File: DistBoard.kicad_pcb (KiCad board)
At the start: 2 copper layers, 63.6 x 50.8 mm, 21 parts, among them J1 22-27-2021, J2 Conn_01x03, J3 Conn_01x03, J4 Conn_01x03, J5 Conn_01x03, U1 TLE2426CDR

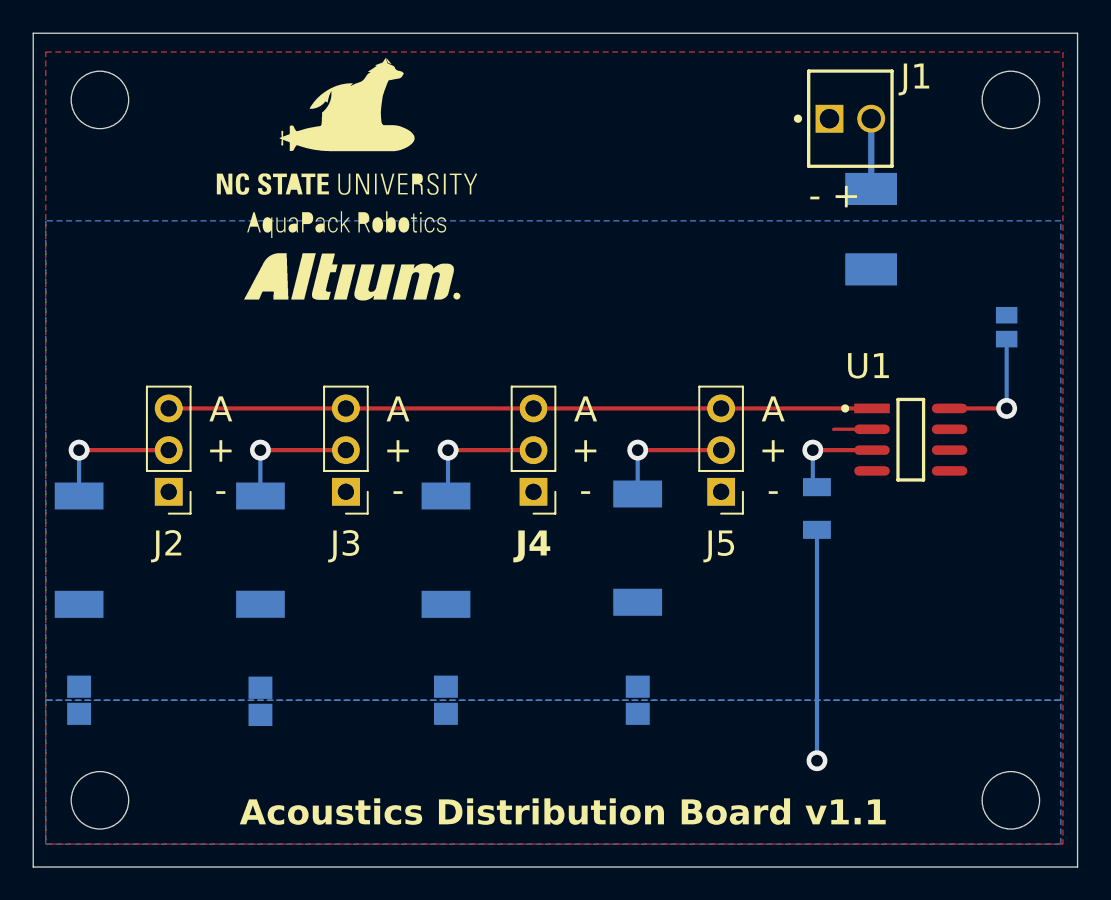
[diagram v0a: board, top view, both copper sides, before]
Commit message: Swap to socket headers and fix drc violations
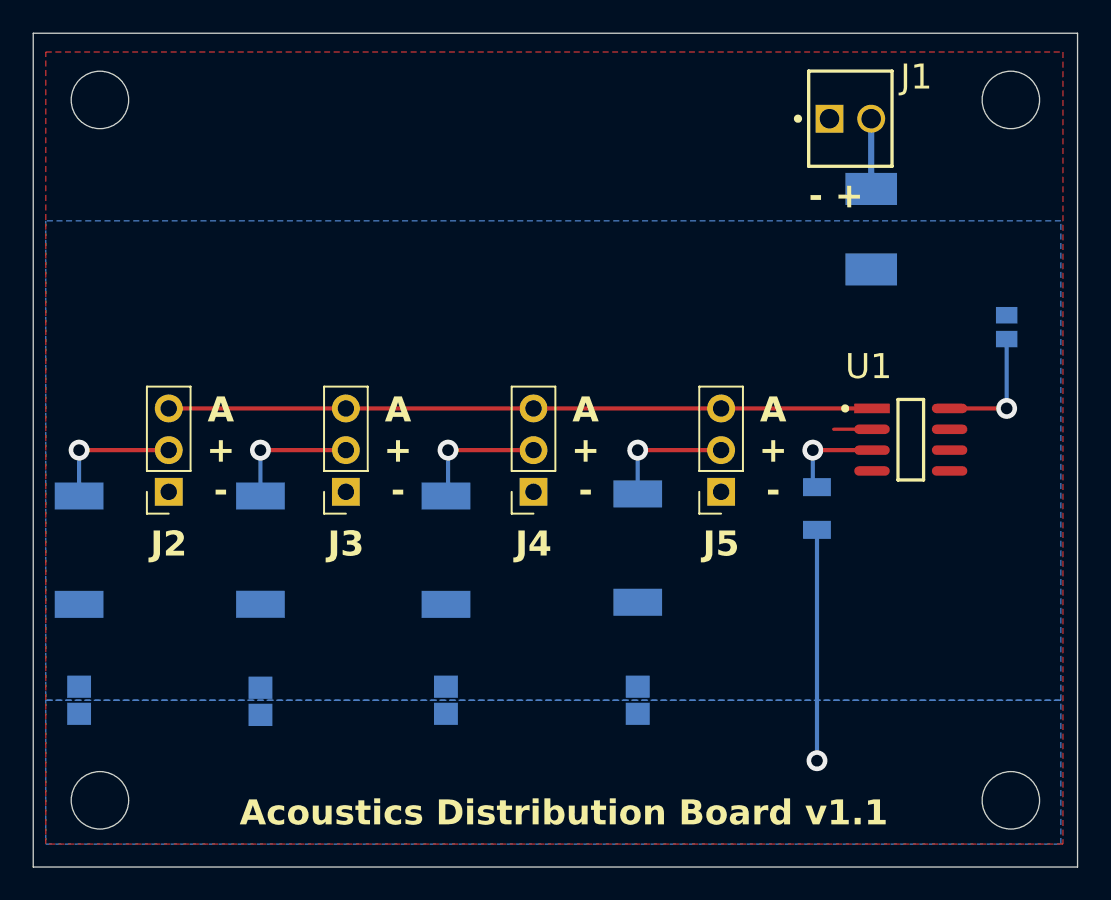
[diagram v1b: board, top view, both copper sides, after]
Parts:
- J2, J3, J4, J5: footprint Connector_PinHeader_2.54mm:PinHeader_1x03_P2.54mm_Vertical -> Connector_PinSocket_2.54mm:PinSocket_1x03_P2.54mm_Vertical

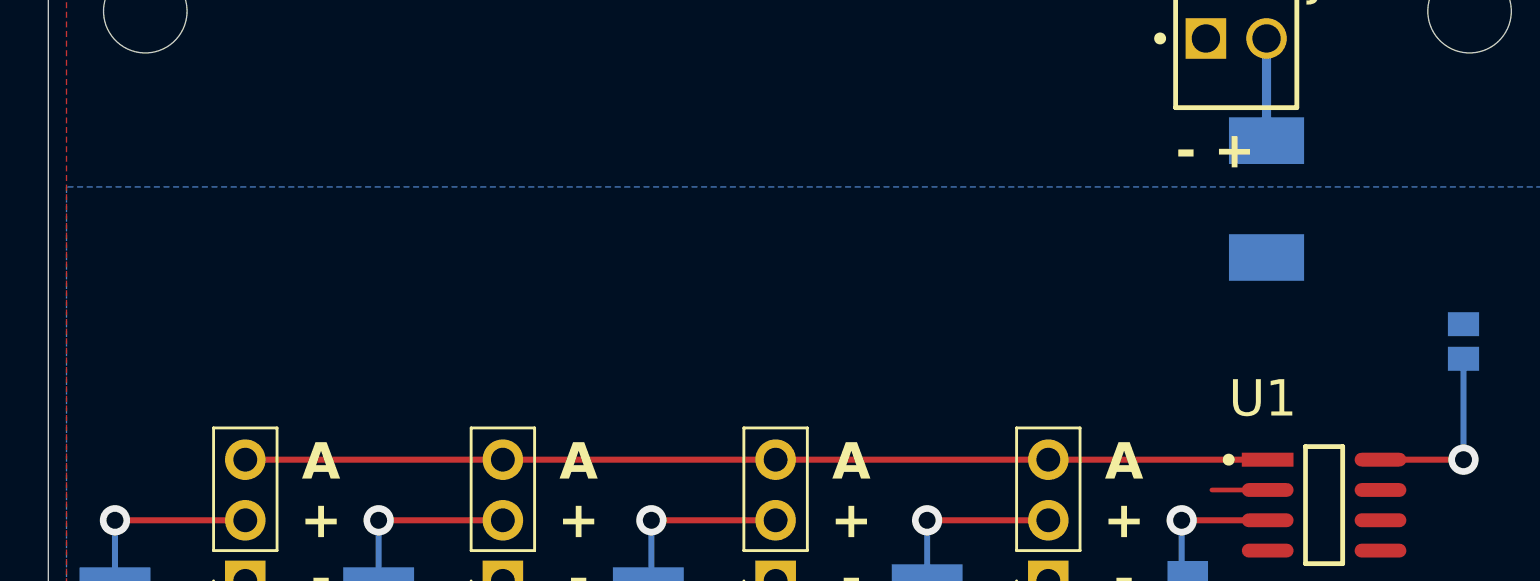
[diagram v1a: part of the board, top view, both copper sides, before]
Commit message: Add logos
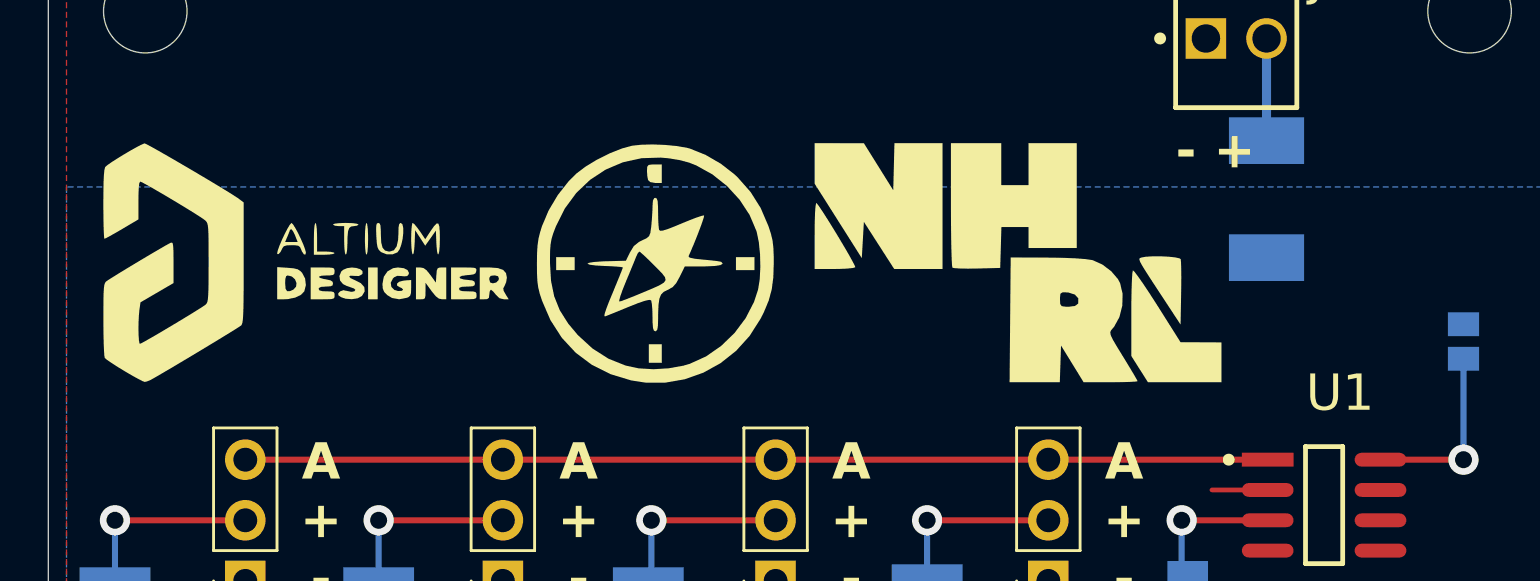
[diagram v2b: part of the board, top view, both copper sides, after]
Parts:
- added G***: LOGO, LOGO, F.Cu at (142.1, 94.2)
- added G***: LOGO, LOGO, F.Cu at (127.5, 94.2)
- added G***: LOGO, LOGO, F.Cu at (157.3, 94.2)
- added G***: LOGO, LOGO, B.Cu at (142.1, 89.1)

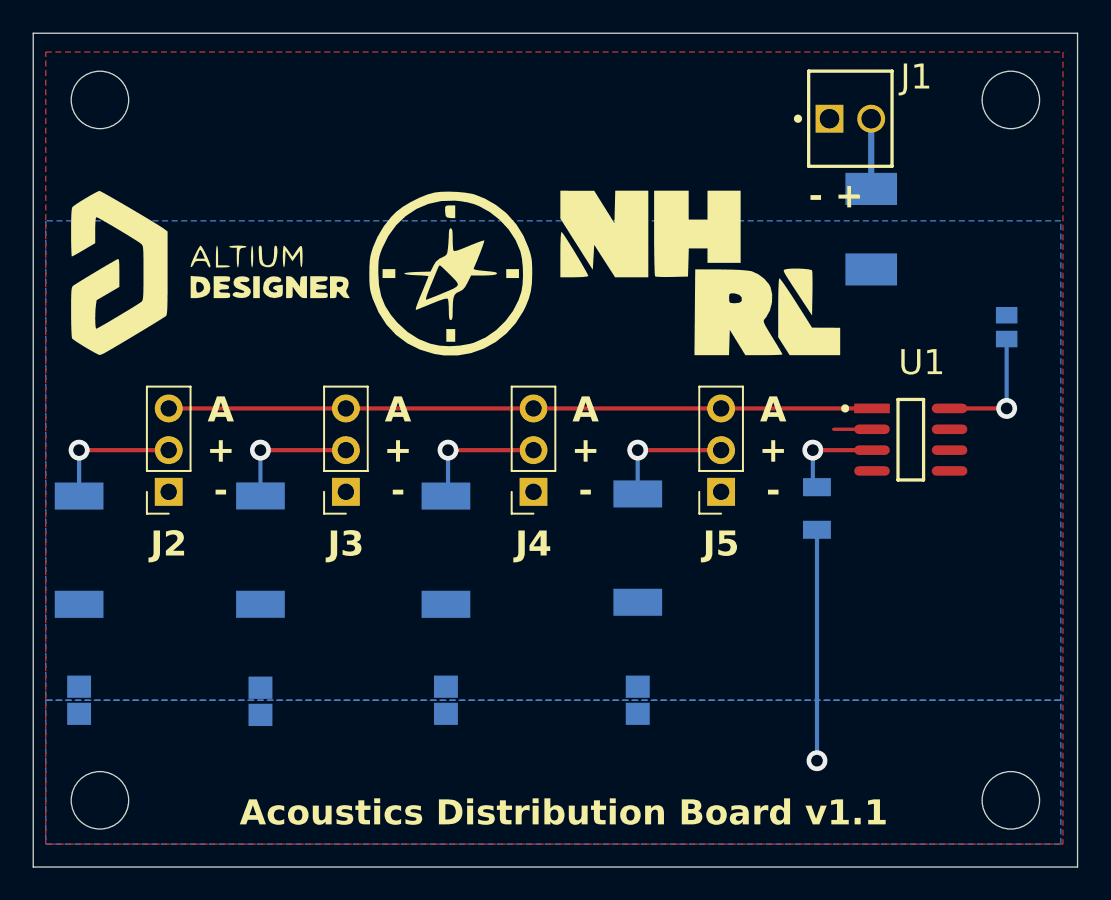
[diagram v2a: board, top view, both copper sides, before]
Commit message: Change capacitor footprints
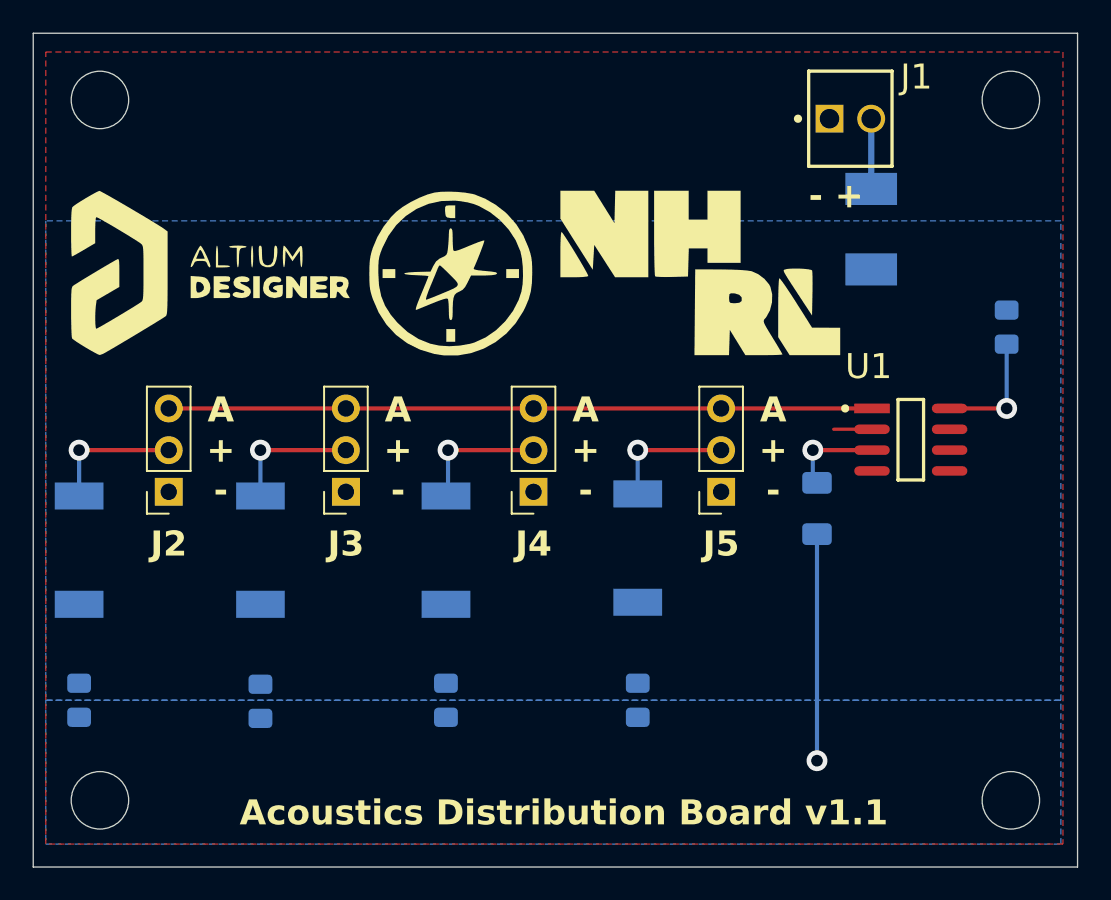
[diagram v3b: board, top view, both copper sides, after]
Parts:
- C1, C2, C3, C4: value GCJ21BR71H105KA01L -> 1uF; footprint AltiumImport:FP-GCJ21B-0_3-IPC_B -> Capacitor_SMD:C_0805_2012Metric_Pad1.18x1.45mm_HandSolder
- C5: value GCD21BR71H104KA01L -> 100nF; footprint AltiumImport:FP-GCD21B-0_15-IPC_C -> Capacitor_SMD:C_0805_2012Metric_Pad1.18x1.45mm_HandSolder
- C6: value C1206C105K5RACTU -> 1uF; footprint AltiumImport:CAPC3216X110X50LL20T25 -> Capacitor_SMD:C_1206_3216Metric_Pad1.33x1.80mm_HandSolder
- F1: value 045201.5MRL -> 1.5A
- F2, F3, F4, F5: value 0459.250UR -> 0.25A
